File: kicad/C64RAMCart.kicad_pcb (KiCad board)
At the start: 2 copper layers, 137 x 126.4 mm, 36 parts, among them J1 C64-Exp-Port_C64-Exp-Port, SW1 SW_SPST, SW2 SW_Push, SW3 SW_SPST, U1 2764, U10 KM62256CLP, U11 KM62256CLP, U2 74LS74, U3 6821, U4 6821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

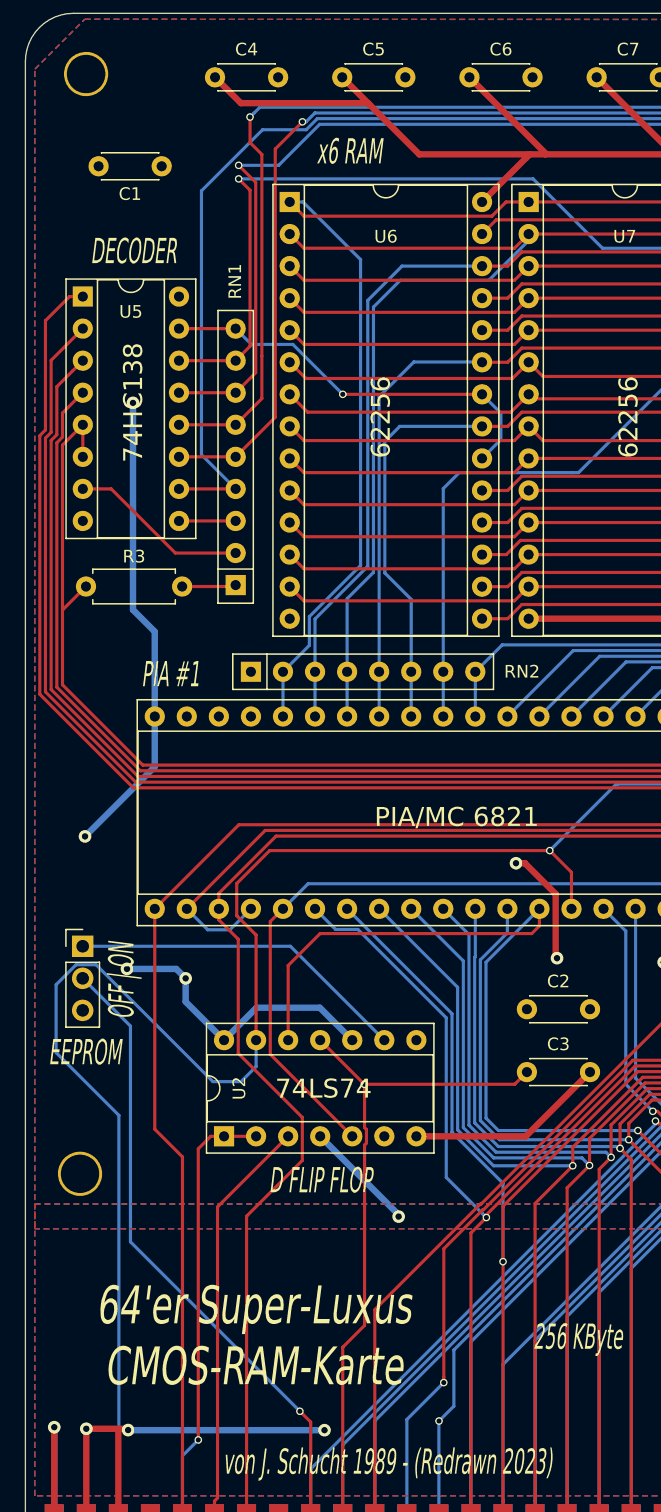
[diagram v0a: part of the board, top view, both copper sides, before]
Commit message: PCB and Schematic tidy
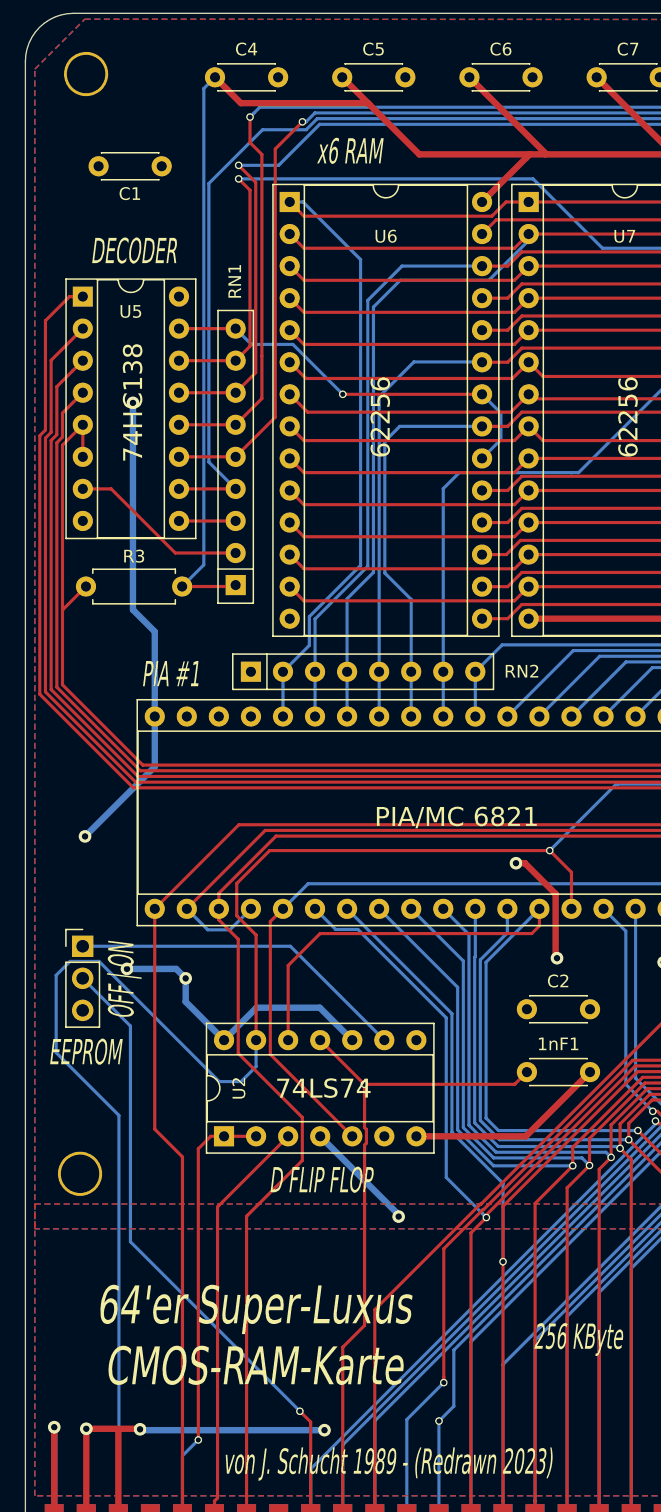
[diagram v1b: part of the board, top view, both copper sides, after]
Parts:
- C1, C2: value C -> 100nF
- R1: value R_Small -> 390
- R2, R3: value R_Small -> 4k7
- RN1: value R_Network08 -> R_6k8_Network08
- RN2: value R_Network07 -> R_6k8_Network07
- renumbered C3 to 1nF1
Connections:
- net a13 renamed Net-(J1-PadJ)
- net a14 renamed Net-(J1-PadH)
- net a15 renamed Net-(J1-PadF)
- R3 pad 2: Net-(R3-Pad2) -> BVcc
- RN1 pad 1: Net-(R3-Pad2) -> BVcc
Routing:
- net BVcc: track 295.5 -> 341.2 mm
- net Net-(R3-Pad2): track 4.29 -> 0.00 mm
- net ~RES: track 277.8 -> 278.5 mm

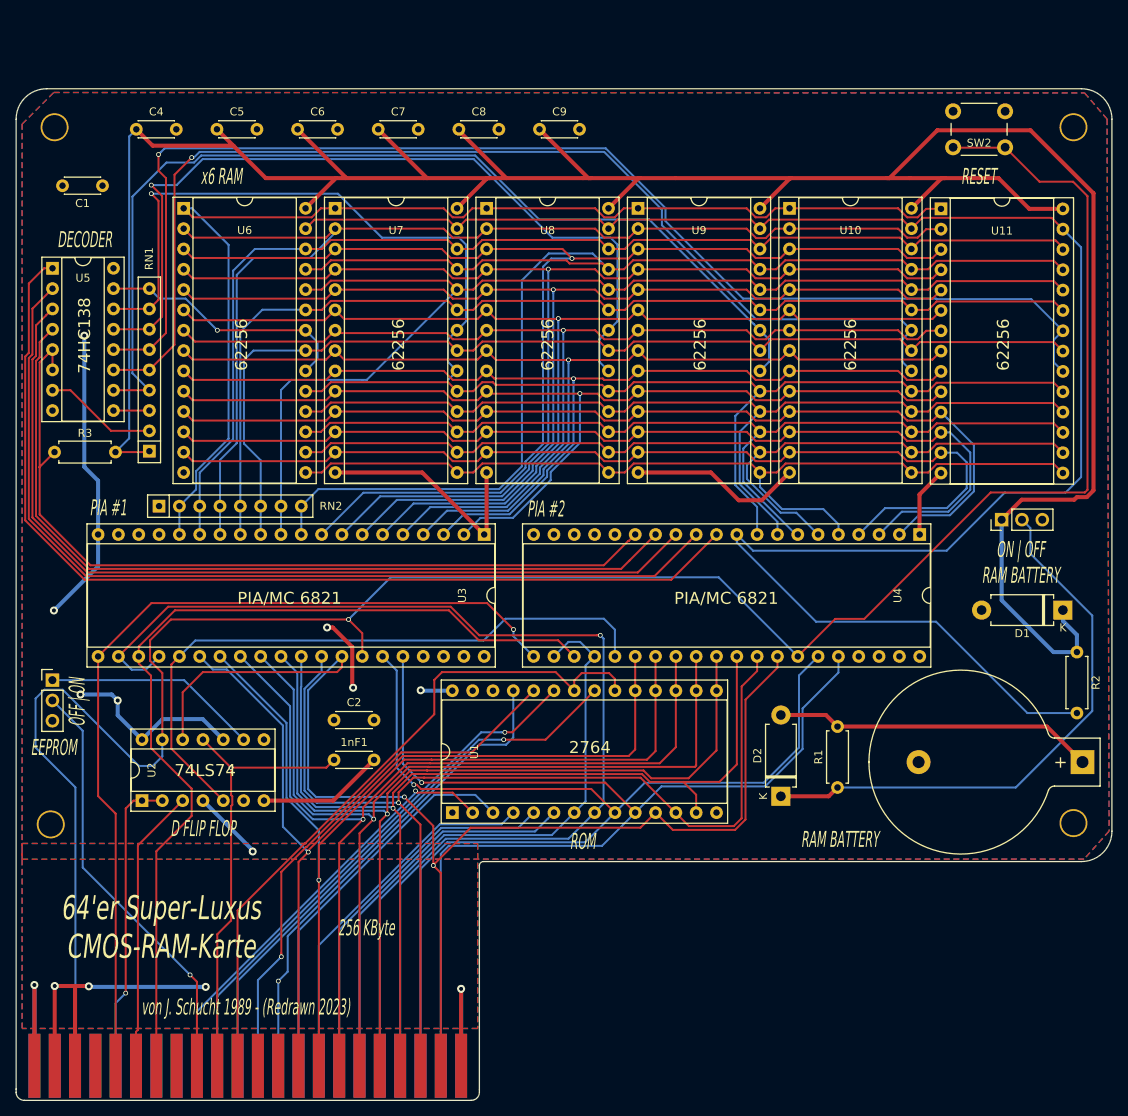
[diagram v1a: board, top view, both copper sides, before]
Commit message: Remaining SRAM added
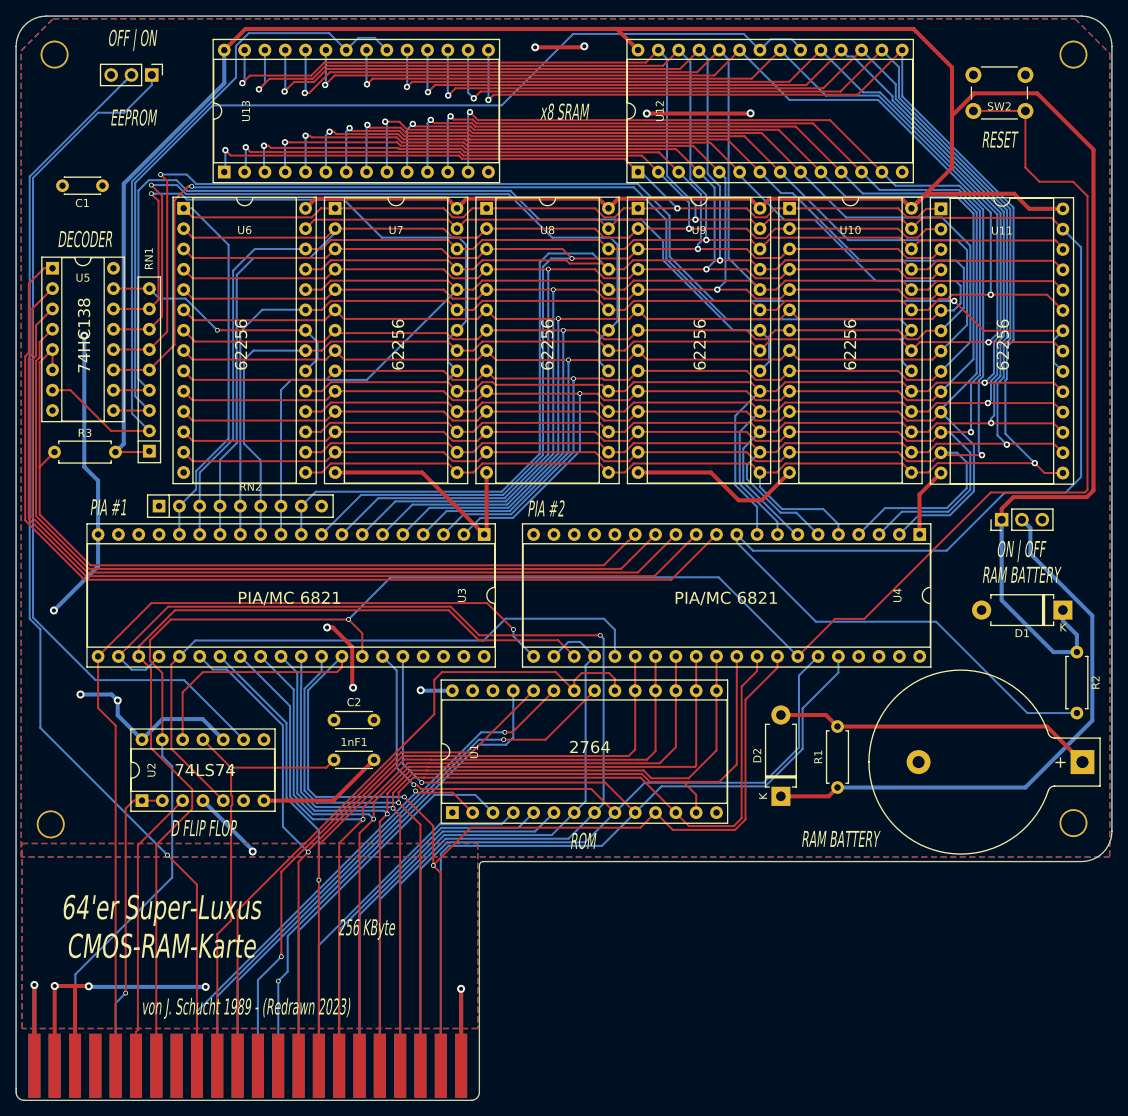
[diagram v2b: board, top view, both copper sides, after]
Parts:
- removed C4, C5, C6, C7, C8, C9: C, Capacitor_THT:C_Disc_D4.3mm_W1.9mm_P5.00mm
- added U12: KM62256CLP, Package_DIP:DIP-28_W15.24mm_Socket, F.Cu at (157.8, 45.7)
- added U13: KM62256CLP, Package_DIP:DIP-28_W15.24mm_Socket, F.Cu at (106.1, 45.7)
- J1: value C64-Exp-Port_C64-Exp-Port -> C64-Exp-Port
- RN2: value R_6k8_Network07 -> R_6k8_Network08; footprint Resistor_THT:R_Array_SIP8 -> Resistor_THT:R_Array_SIP9
- moved SW3 76.7 mm to (97.0, 33.6), turned to 270 degrees
- moved H1 9.08 mm to (84.9, 31.0)
- moved H2 9.08 mm to (212.2, 31.0)
- moved SW2 5.20 mm to (206.2, 38.1)
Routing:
- net y6: track 4.49 -> 126.7 mm
- net dr3: track 114.1 -> 234.1 mm, vias 0 -> 2
- net dr4: track 115.1 -> 232.2 mm, vias 0 -> 2
- net dr5: track 115.9 -> 230.6 mm, vias 0 -> 2
- net dr2: track 122.1 -> 235.3 mm, vias 0 -> 2
- net dr6: track 117.7 -> 230.5 mm, vias 0 -> 2
- net dr7: track 119.6 -> 230.8 mm, vias 0 -> 2
- net ar10: track 130.4 -> 240.5 mm, vias 0 -> 2
- net dr1: track 122.4 -> 232.4 mm, vias 0 -> 2
- net ar11: track 133.9 -> 242.7 mm, vias 0 -> 2
- net dr0: track 122.5 -> 229.0 mm, vias 0 -> 1
- net ar0: track 125.3 -> 230.3 mm, vias 1 -> 2
- net ar1: track 128.9 -> 232.1 mm, vias 1 -> 2
- net ar2: track 133.2 -> 234.7 mm, vias 1 -> 2
- net ar3: track 139.0 -> 237.8 mm, vias 1 -> 2
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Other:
- board size 137 x 126.4 mm -> 137 x 135.5 mm
- board text added: "x8 SRAM"
- board text removed: "x6 RAM"
